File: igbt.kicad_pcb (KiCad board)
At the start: 2 copper layers, 94 parts, among them J1 PWM, J10 Motor, J2 PwrGate_A, J3 PwrGate_B, J4 PwrGate_C, J5 PWM, J6 PWM, J7 Sense_AC_B, J8 Sense_AC_A, J9 DC_Sense, Q1 IRG4PF50W, Q2 IRG4PF50W, Q3 IRG4PF50W, Q4 IRG4PF50W, Q5 IRG4PF50W, Q6 IRG4PF50W, U1 ACS758xCB-050B-PFF, U10 TC4420, U11 6N137, U12 TC4420, U13 6N137, U14 TC4420, U2 ACS758xCB-050B-PFF, U3 6N137, U4 TC4420, U5 6N137, U6 TC4420, U7 6N137, U8 TC4420, U9 6N137

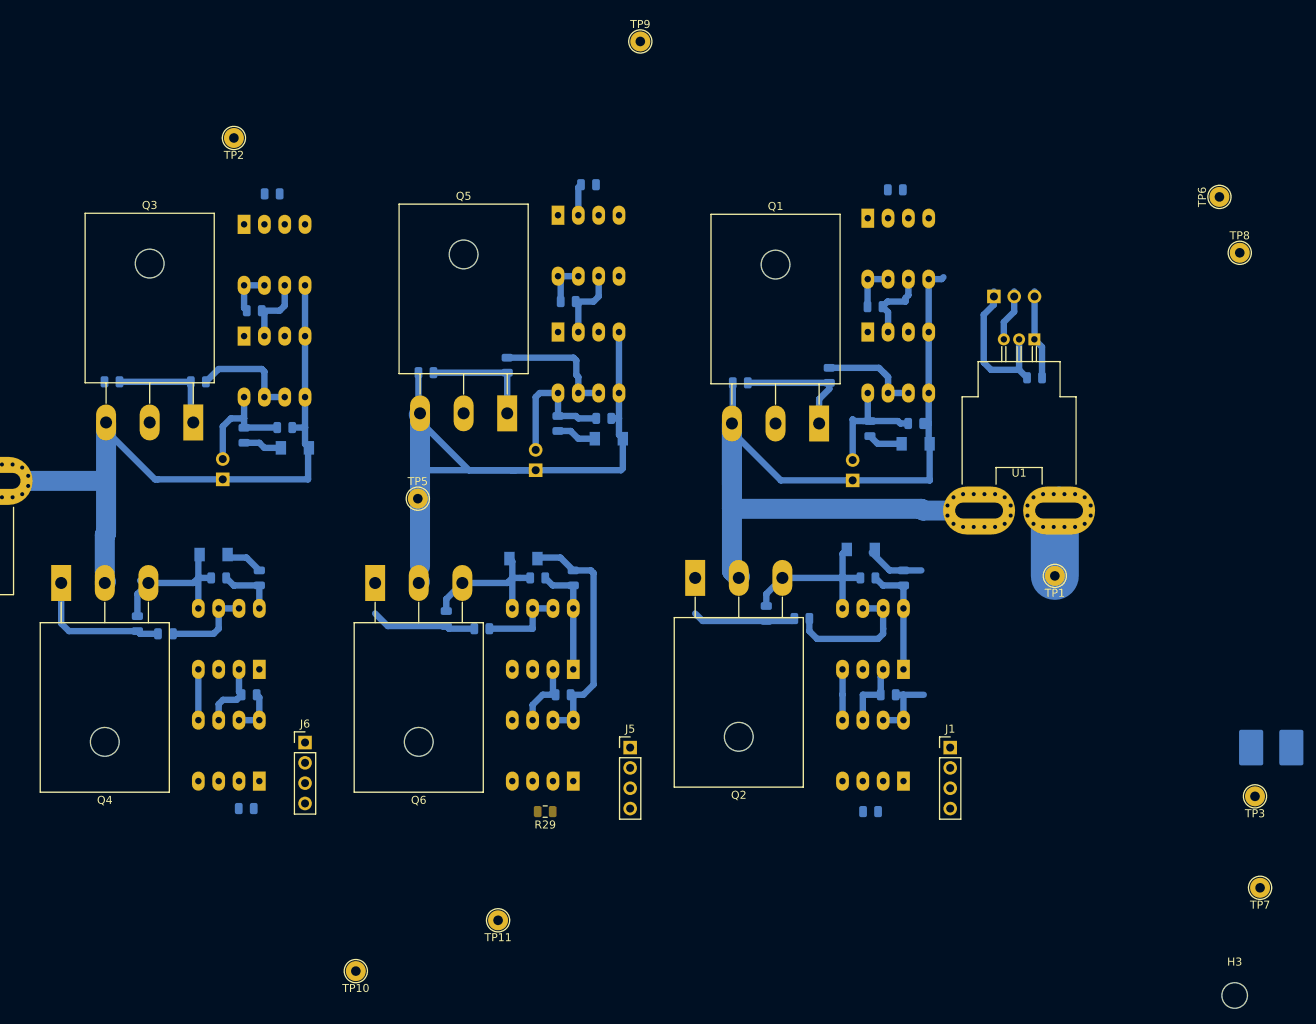
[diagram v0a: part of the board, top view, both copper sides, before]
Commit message: Bus capacitors
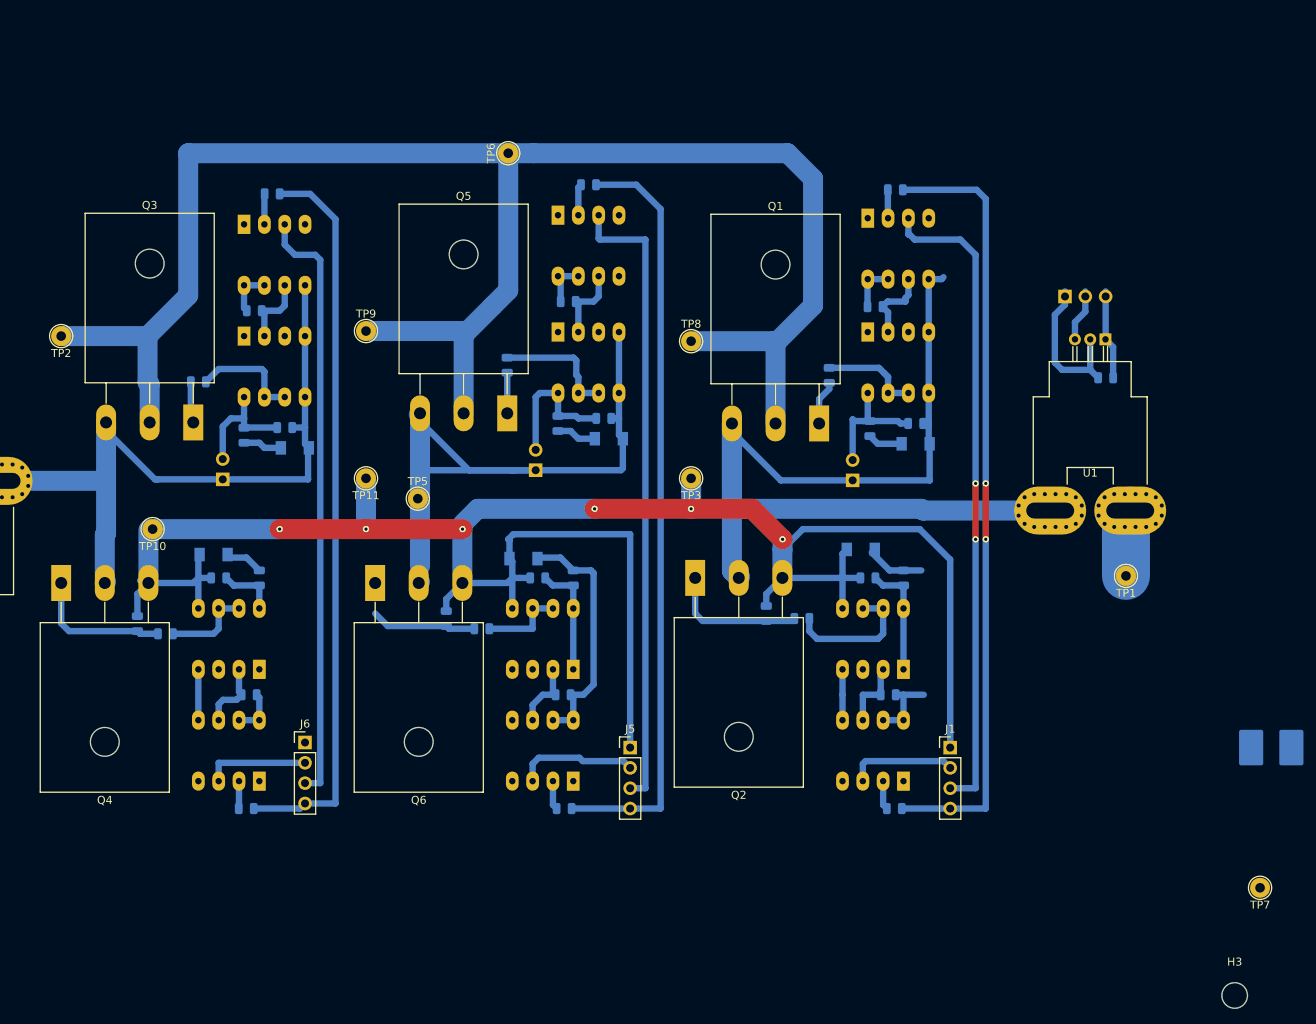
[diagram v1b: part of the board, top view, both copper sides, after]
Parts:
- removed R1, R3, R5: R, Capacitor_SMD:C_0805_2012Metric
- R29: moved to B.Cu
- moved TP6 89.1 mm to (148.0, 50.2)
- moved TP3 80.9 mm to (170.8, 90.8)
- moved TP8 69.5 mm to (170.8, 73.7)
- moved TP10 60.8 mm to (103.5, 97.2)
- moved TP11 57.7 mm to (130.2, 90.8)
- moved TP9 49.9 mm to (130.2, 72.4)
- moved TP2 32.9 mm to (92.1, 73.0)
- moved U1 8.89 mm to (222.6, 73.4)
- moved C4 8.89 mm to (222.6, 78.2)
- moved J8 8.89 mm to (217.6, 68.1)
- moved TP1 8.89 mm to (225.2, 103.0)
- moved R23 2.99 mm to (196.2, 132.1), turned to 0 degrees
- moved R29 2.39 mm to (154.9, 132.1), turned to 0 degrees
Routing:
- net Net-(Q1-Pad2): track 0.71 -> 215.2 mm
- net /DC_Link_GND: track 74.4 -> 276.8 mm, vias 0 -> 6
- net /TopDriver/PowerLed: track 0.00 -> 97.5 mm, vias 0 -> 2
- net /sheet5F5616DC/PowerLed: track 0.00 -> 95.4 mm
- net /sheet5F55AA82/PowerLed: track 0.00 -> 91.8 mm
- net /TopDriver/Cathode: track 0.00 -> 81.3 mm, vias 0 -> 2
- net /sheet5F5616DC/Cathode: track 0.00 -> 79.3 mm
- net /sheet5F55AA82/Cathode: track 0.00 -> 75.1 mm
- net /sheet5F64C50D/Cathode: track 0.00 -> 15.2 mm
- net /sheet5F641D5F/Cathode: track 0.00 -> 13.6 mm
- net /sheet5F647249/Cathode: track 0.00 -> 13.1 mm
- net Net-(Q1-Pad1): track 15.8 -> 5.61 mm
- net Net-(Q5-Pad1): track 14.3 -> 5.08 mm
- net Net-(Q3-Pad1): track 14.1 -> 5.21 mm
- net /sheet5F5616DC/Source: track 86.9 -> 82.0 mm
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
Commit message: Reroute driver tracks
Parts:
- removed J9: DC_Sense, Connector_PinHeader_2.54mm:PinHeader_1x02_P2.54mm_Vertical
- removed R32: 1k, Resistor_SMD:R_2816_7142Metric
- removed R8: 100k, Resistor_SMD:R_2816_7142Metric
- removed TP7: DC_GND, TestPoint:TestPoint_THTPad_D2.5mm_Drill1.2mm
- removed U1: ACS758xCB-050B-PFF, Sensor_Current:Allegro_CB_PFF
- J1, J5, J6: moved to B.Cu
- moved H1 103.5 mm to (48.9, 153.7)
- moved H2 103.5 mm to (36.2, 153.0)
- moved TP14 86.4 mm to (84.5, 72.4)
- moved J10 85.7 mm to (85.1, 60.3)
- moved TP12 85.7 mm to (85.1, 55.2)
- moved TP13 85.7 mm to (80.0, 63.5)
- moved TP4 10.2 mm to (78.4, 74.4)
- moved U2 10.2 mm to (82.2, 103.6)
- moved C5 6.38 mm to (83.2, 106.0)
- moved C4 5.75 mm to (216.9, 78.9)
- moved TP1 5.75 mm to (219.5, 103.6)
- moved J8 5.75 mm to (211.8, 68.7)
- moved J5 3.17 mm to (160.0, 124.5), turned to 180 degrees
- moved J6 2.01 mm to (120.7, 124.5), turned to 180 degrees
- moved J1 1.91 mm to (201.3, 124.5), turned to 180 degrees
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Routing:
- net /DC_Link_GND: track 276.8 -> 342.3 mm
- net Net-(J7-Pad2): track 6.99 -> 40.4 mm
- net /TopDriver/Cathode: track 81.3 -> 108.1 mm, vias 2 -> 0
- net /TopDriver/PowerLed: track 97.5 -> 116.1 mm, vias 2 -> 0
- net Net-(C5-Pad2): track 9.44 -> 19.4 mm
- net /TopDriver/Source: track 135.0 -> 126.1 mm
- net /sheet5F5616DC/Source: track 82.0 -> 88.7 mm
- net /sheet5F55AA82/Source: track 87.7 -> 81.3 mm
- net Net-(D4-Pad1): track 16.4 -> 11.6 mm
- net Net-(Q1-Pad2): track 215.2 -> 211.4 mm
- net Net-(Q6-Pad1): track 13.2 -> 17.0 mm
- net /sheet5F64C50D/Cathode: track 15.2 -> 12.0 mm
- net Net-(J10-Pad3): track 7.50 -> 5.33 mm
- net /sheet5F55AA82/Cathode: track 75.1 -> 76.9 mm
- net /sheet5F641D5F/Cathode: track 13.6 -> 12.0 mm
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
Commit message: Board edge
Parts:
- added TP7: DC_GND, TestPoint:TestPoint_THTPad_D2.5mm_Drill1.2mm, F.Cu at (144.8, 94.0)
- added U1: ACS758xCB-050B-PFF, Sensor_Current:Allegro_CB_PFF, F.Cu at (211.5, 73.7)
- J8: moved to F.Cu
- moved H4 214.0 mm to (76.2, 49.5)
- moved H2 190.7 mm to (225.4, 129.5)
- moved H3 106.8 mm to (225.4, 49.5)
- moved H1 36.4 mm to (76.2, 129.5)
- moved D2 25.2 mm to (110.0, 64.5), turned to 180 degrees
- moved D1 24.8 mm to (186.9, 64.8), turned to 180 degrees
- moved D3 23.9 mm to (149.4, 64.8), turned to 180 degrees
- moved D5 22.1 mm to (103.6, 121.2), turned to 0 degrees
- moved D4 20.7 mm to (185.5, 119.3), turned to 270 degrees
- moved C1 19.5 mm to (186.1, 69.2), turned to 0 degrees
- moved R28 18.8 mm to (102.0, 114.8), turned to 270 degrees
- moved D6 18.1 mm to (145.0, 118.2), turned to 270 degrees
- moved R19 17.4 mm to (111.8, 68.3), turned to 90 degrees
- moved R12 17.0 mm to (189.2, 68.1), turned to 90 degrees
- moved C2 16.4 mm to (109.2, 72.1), turned to 0 degrees
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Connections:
- U10 pad 3: Net-(U10-Pad3) -> (no net)
- U11 pad 1: Net-(U11-Pad1) -> (no net)
- U11 pad 4: Net-(U11-Pad4) -> (no net)
- U12 pad 3: Net-(U12-Pad3) -> (no net)
- U13 pad 1: Net-(U13-Pad1) -> (no net)
- U13 pad 4: Net-(U13-Pad4) -> (no net)
- U14 pad 3: Net-(U14-Pad3) -> (no net)
- U3 pad 1: Net-(U3-Pad1) -> (no net)
- U3 pad 4: Net-(U3-Pad4) -> (no net)
- U4 pad 3: Net-(U4-Pad3) -> (no net)
- U5 pad 1: Net-(U5-Pad1) -> (no net)
- U5 pad 4: Net-(U5-Pad4) -> (no net)
- U6 pad 3: Net-(U6-Pad3) -> (no net)
- U7 pad 1: Net-(U7-Pad1) -> (no net)
- U7 pad 4: Net-(U7-Pad4) -> (no net)
- U8 pad 3: Net-(U8-Pad3) -> (no net)
- U9 pad 1: Net-(U9-Pad1) -> (no net)
- U9 pad 4: Net-(U9-Pad4) -> (no net)
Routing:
- net /sheet5F5616DC/Source: track 88.7 -> 118.5 mm
- net /sheet5F55AA82/Source: track 81.3 -> 103.2 mm
- net Net-(D5-Pad1): track 10.5 -> 31.2 mm, vias 0 -> 2
- net /sheet5F647249/Power: track 7.43 -> 27.0 mm
- net /sheet5F55AA82/Power: track 15.1 -> 31.7 mm, vias 0 -> 2
- net /TopDriver/Power: track 15.8 -> 32.2 mm, vias 0 -> 2
- net /TopDriver/Source: track 126.1 -> 141.9 mm
- net Net-(D4-Pad1): track 11.6 -> 26.0 mm, vias 0 -> 2
- net /sheet5F5616DC/Power: track 17.4 -> 26.7 mm, vias 0 -> 2
- net /sheet5F641D5F/Power: track 14.4 -> 23.3 mm
- net /sheet5F64C50D/Power: track 14.4 -> 22.3 mm
- net Net-(J8-Pad2): track 6.53 -> 13.9 mm
- net /DC_Link_GND: track 342.3 -> 348.2 mm
- net Net-(D6-Pad1): track 31.1 -> 25.7 mm, vias 0 -> 2
- net /TopDriver/PowerLed: track 116.1 -> 120.7 mm
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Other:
- board outline added: 159.4 x 90.2 mm

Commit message: Fill flooded
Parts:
- J8: moved to B.Cu
- moved TP13 8.91 mm to (88.9, 64.1)
- moved R25 4.51 mm to (181.0, 114.5)
- moved R31 4.39 mm to (141.0, 114.9)
- moved D6 3.74 mm to (142.9, 121.3), turned to 0 degrees
- moved D4 3.26 mm to (182.9, 121.3), turned to 0 degrees
- moved R17 1.62 mm to (149.2, 77.5), turned to 0 degrees
- moved J4 1.02 mm to (151.4, 90.8)
- turned J8 to 180 degrees
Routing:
- net Net-(D4-Pad1): track 26.0 -> 34.2 mm
- net Net-(J7-Pad2): track 40.4 -> 48.3 mm
- net /sheet5F5616DC/Source: track 118.5 -> 110.6 mm
- net Net-(C5-Pad1): track 15.3 -> 22.4 mm
- net Net-(D6-Pad1): track 25.7 -> 32.6 mm
- net Net-(C4-Pad2): track 24.0 -> 29.3 mm
- net /TopDriver/Source: track 141.9 -> 147.1 mm
- net /sheet5F64C50D/Power: track 22.3 -> 27.1 mm
- net /sheet5F641D5F/Power: track 23.3 -> 27.8 mm
- net /DC_Link_GND: track 348.2 -> 352.0 mm
- net /TopDriver/PowerLed: track 120.7 -> 123.9 mm
- net /TopDriver/Cathode: track 108.1 -> 110.5 mm
- net /sheet5F5616DC/Gate: track 13.5 -> 11.8 mm
- net /sheet5F55AA82/PowerLed: track 90.3 -> 92.0 mm
- net /sheet5F55AA82/Gate: track 13.8 -> 12.3 mm
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- added copper zone on B.Cu, net (none)
- added copper zone on B.Cu, net /DC_Link_GND
- added copper zone on B.Cu, net Net-(Q1-Pad2)

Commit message: Use adum1300
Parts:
- removed D4, D5, D6: 5V1, Diode_SMD:D_MiniMELF
- removed J3: PwrGate_B, Connector_PinHeader_2.54mm:PinHeader_1x02_P2.54mm_Vertical
- removed J4: PwrGate_C, Connector_PinHeader_2.54mm:PinHeader_1x02_P2.54mm_Vertical
- removed J5, J6: PWM, Connector_PinHeader_2.54mm:PinHeader_1x04_P2.54mm_Vertical
- removed R12, R18, R19, R21, R22, R24, R25, R27, R28, R30, R31, R9: 1k, Resistor_SMD:R_0805_2012Metric
- removed R13, R14, R4, R6: R, Capacitor_SMD:C_0805_2012Metric
- removed R15, R20, R23, R26, R29, R7: 330, Resistor_SMD:R_0805_2012Metric
- removed TP10: DC_CapB_N, TestPoint:TestPoint_THTPad_D2.5mm_Drill1.2mm
- removed TP11: DC_CapC_N, TestPoint:TestPoint_THTPad_D2.5mm_Drill1.2mm
- removed TP2: DC_CapB_P, TestPoint:TestPoint_THTPad_D2.5mm_Drill1.2mm
- removed TP3: DC_CapA_N, TestPoint:TestPoint_THTPad_D2.5mm_Drill1.2mm
- removed TP5: C, TestPoint:TestPoint_THTPad_D2.5mm_Drill1.2mm
- removed TP6: DC_BUS, TestPoint:TestPoint_THTPad_D2.5mm_Drill1.2mm
- removed TP7: DC_GND, TestPoint:TestPoint_THTPad_D2.5mm_Drill1.2mm
- removed TP8: DC_CapA_P, TestPoint:TestPoint_THTPad_D2.5mm_Drill1.2mm
- removed TP9: DC_CapC_P, TestPoint:TestPoint_THTPad_D2.5mm_Drill1.2mm
- removed U10, U12, U14, U8: TC4420, Package_DIP:DIP-8_W7.62mm_LongPads
- removed U11, U13, U9: 6N137, Package_DIP:DIP-8_W7.62mm_LongPads
- added J9: DC_Sense, Connector_PinHeader_2.54mm:PinHeader_1x02_P2.54mm_Vertical, F.Cu at (55.2, 42.5)
- added R1: R, Capacitor_SMD:C_0805_2012Metric, B.Cu at (94.0, 108.0)
- added R32: 1k, Resistor_SMD:R_2816_7142Metric, B.Cu at (49.4, 45.0)
- added R8: 100k, Resistor_SMD:R_2816_7142Metric, B.Cu at (49.4, 40.0)
- D1, D2, D3: value 5V1 -> DIODE; footprint Diode_SMD:D_MiniMELF -> Diode_THT:D_A-405_P2.54mm_Vertical_KathodeUp
- J1: footprint Connector_PinHeader_2.54mm:PinHeader_1x04_P2.54mm_Vertical -> Connector_PinHeader_2.54mm:PinHeader_1x08_P2.54mm_Vertical
- J2: value PwrGate_A -> V_Gate
- U3: value 6N137 -> ADum1300; footprint Package_DIP:DIP-8_W7.62mm_LongPads -> Package_SO:SOIC-16W_7.5x10.3mm_P1.27mm
- U4: value TC4420 -> ADum1300; footprint Package_DIP:DIP-8_W7.62mm_LongPads -> Package_SO:SOIC-16W_7.5x10.3mm_P1.27mm
- U5, U7: value 6N137 -> IR2110; footprint Package_DIP:DIP-8_W7.62mm_LongPads -> Package_SO:SOIC-16W_7.5x10.3mm_P1.27mm
- U6: value TC4420 -> IR2110; footprint Package_DIP:DIP-8_W7.62mm_LongPads -> Package_SO:SOIC-16W_7.5x10.3mm_P1.27mm
- moved H2 168.8 mm to (124.5, -5.71)
- moved H1 154.7 mm to (138.4, -12.1)
- moved H3 129.3 mm to (108.0, -4.45)
- moved C6 106.1 mm to (91.4, 102.9)
- moved R2 87.6 mm to (94.0, 92.1), turned to 270 degrees
- moved U3 73.3 mm to (150.9, 118.4), turned to 90 degrees
- moved C3 63.3 mm to (91.4, 99.1), turned to 270 degrees
- moved H4 61.3 mm to (96.5, -8.26)
- moved C1 58.7 mm to (134.9, 97.9), turned to 270 degrees
- moved J10 56.0 mm to (29.2, 64.1)
- moved TP12 56.0 mm to (29.2, 59.1)
- moved TP13 56.0 mm to (33.0, 67.9)
- moved C4 55.3 mm to (267.1, 82.0)
- moved J8 55.3 mm to (273.1, 74.9)
- moved TP1 55.3 mm to (269.2, 104.1)
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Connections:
- C1 pad 1: /TopDriver/Source -> Net-(C1-Pad1)
- C1 pad 2: /TopDriver/Power -> Net-(C1-Pad2)
- C2 pad 1: /sheet5F55AA82/Source -> Net-(C2-Pad1)
- C2 pad 2: /sheet5F55AA82/Power -> /DC_Link_GND
- C3 pad 1: /sheet5F5616DC/Source -> Net-(C3-Pad1)
- C3 pad 2: /sheet5F5616DC/Power -> Net-(C3-Pad2)
- C6 pad 1: /DC_Link_GND -> Net-(C2-Pad1)
- C6 pad 2: /sheet5F641D5F/Power -> /DC_Link_GND
- C7 pad 1: /DC_Link_GND -> Net-(C7-Pad1)
- C7 pad 2: /sheet5F647249/Power -> Net-(C7-Pad2)
- C8 pad 1: /DC_Link_GND -> Net-(C2-Pad1)
- C8 pad 2: /sheet5F64C50D/Power -> /DC_Link_GND
- D1 pad 1: Net-(D1-Pad1) -> Net-(C2-Pad1)
- D1 pad 2: /TopDriver/Source -> Net-(C1-Pad1)
- D2 pad 1: Net-(D2-Pad1) -> Net-(C2-Pad1)
- D2 pad 2: /sheet5F55AA82/Source -> Net-(C3-Pad1)
- D3 pad 1: Net-(D3-Pad1) -> Net-(C2-Pad1)
- D3 pad 2: /sheet5F5616DC/Source -> Net-(C7-Pad1)
- J1 pad 1: /DC_Link_GND -> Net-(J1-Pad1)
- J1 pad 2: /sheet5F641D5F/Cathode -> Net-(J1-Pad2)
- J1 pad 3: /TopDriver/Cathode -> Net-(J1-Pad3)
- J1 pad 4: /TopDriver/PowerLed -> Net-(J1-Pad4)
- J2 pad 1: /TopDriver/Source -> Net-(J2-Pad1)
- J2 pad 2: /TopDriver/Power -> Net-(C2-Pad1)
- Q1 pad 3: /TopDriver/Source -> Net-(C1-Pad2)
- Q2 pad 2: /TopDriver/Source -> Net-(C1-Pad2)
- Q3 pad 3: /sheet5F55AA82/Source -> Net-(C3-Pad2)
- Q4 pad 2: /sheet5F55AA82/Source -> Net-(C3-Pad2)
- Q5 pad 3: /sheet5F5616DC/Source -> Net-(C7-Pad2)
- Q6 pad 2: /sheet5F5616DC/Source -> Net-(C7-Pad2)
- R10 pad 2: /sheet5F641D5F/Gate -> Net-(R10-Pad2)
- R11 pad 2: /TopDriver/Gate -> Net-(R11-Pad2)
- R16 pad 2: /sheet5F64C50D/Gate -> Net-(R16-Pad2)
- R17 pad 2: /sheet5F5616DC/Gate -> Net-(R17-Pad2)
- R2 pad 1: Net-(Q2-Pad1) -> Net-(Q3-Pad1)
- R2 pad 2: /DC_Link_GND -> Net-(R2-Pad2)
- U1 pad 4: /TopDriver/Source -> Net-(C1-Pad2)
- U2 pad 4: /sheet5F55AA82/Source -> Net-(C3-Pad2)
- U3 pad 1: (no net) -> Net-(J1-Pad8)
- U3 pad 2: Net-(R7-Pad1) -> Net-(J1-Pad8)
- U3 pad 3: /TopDriver/Cathode -> Net-(J1-Pad4)
- U3 pad 4: (no net) -> Net-(J1-Pad3)
- U3 pad 5: /TopDriver/Source -> Net-(J1-Pad2)
- U3 pad 6: Net-(R9-Pad2) -> Net-(U3-Pad6)
- U3 pad 7: Net-(D1-Pad1) -> Net-(U3-Pad7)
- U3 pad 8: Net-(D1-Pad1) -> Net-(J1-Pad1)
- U4 pad 1: /TopDriver/Power -> Net-(J1-Pad8)
- U4 pad 2: Net-(R9-Pad2) -> Net-(J1-Pad1)
- U4 pad 3: (no net) -> Net-(J1-Pad7)
- U4 pad 4: /TopDriver/Source -> Net-(J1-Pad6)
- U4 pad 5: /TopDriver/Source -> Net-(J1-Pad5)
- U4 pad 6: /TopDriver/Gate -> Net-(U4-Pad6)
- U4 pad 7: /TopDriver/Gate -> Net-(U4-Pad7)
- U4 pad 8: /TopDriver/Power -> Net-(J1-Pad1)
- U5 pad 1: (no net) -> Net-(R10-Pad2)
- U5 pad 2: Net-(R15-Pad1) -> /DC_Link_GND
- U5 pad 3: /sheet5F55AA82/Cathode -> Net-(C2-Pad1)
- U5 pad 4: (no net) -> Net-(U5-Pad4)
- U5 pad 5: /sheet5F55AA82/Source -> Net-(C1-Pad2)
- U5 pad 6: Net-(R18-Pad2) -> Net-(C1-Pad1)
- U5 pad 7: Net-(D2-Pad1) -> Net-(R11-Pad2)
- U5 pad 8: Net-(D2-Pad1) -> Net-(U5-Pad8)
- U6 pad 1: /sheet5F55AA82/Power -> Net-(R1-Pad2)
- U6 pad 2: Net-(R18-Pad2) -> /DC_Link_GND
- U6 pad 3: (no net) -> Net-(C2-Pad1)
- U6 pad 4: /sheet5F55AA82/Source -> Net-(U6-Pad4)
- U6 pad 5: /sheet5F55AA82/Source -> Net-(C3-Pad2)
- U6 pad 6: /sheet5F55AA82/Gate -> Net-(C3-Pad1)
- U6 pad 7: /sheet5F55AA82/Gate -> Net-(R2-Pad2)
- U6 pad 8: /sheet5F55AA82/Power -> Net-(U6-Pad8)
- U7 pad 1: (no net) -> Net-(R16-Pad2)
- U7 pad 2: Net-(R20-Pad1) -> /DC_Link_GND
- U7 pad 3: /sheet5F5616DC/Cathode -> Net-(C2-Pad1)
- U7 pad 4: (no net) -> Net-(U7-Pad4)
- U7 pad 5: /sheet5F5616DC/Source -> Net-(C7-Pad2)
- U7 pad 6: Net-(R21-Pad2) -> Net-(C7-Pad1)
- U7 pad 7: Net-(D3-Pad1) -> Net-(R17-Pad2)
- U7 pad 8: Net-(D3-Pad1) -> Net-(U7-Pad8)
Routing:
- net /DC_Link_GND: track 352.0 -> 168.0 mm, vias 6 -> 0
- net Net-(Q1-Pad2): track 211.4 -> 63.2 mm
- net /TopDriver/Source: track 147.1 -> 0.00 mm
- net /TopDriver/PowerLed: track 123.9 -> 0.00 mm
- net Net-(C2-Pad1): track 0.00 -> 113.9 mm, vias 0 -> 4
- net /sheet5F5616DC/Source: track 110.6 -> 0.00 mm
- net /TopDriver/Cathode: track 110.5 -> 0.00 mm
- net Net-(J2-Pad1): track 0.00 -> 107.7 mm, vias 0 -> 4
- net /sheet5F55AA82/Source: track 103.2 -> 0.00 mm
- net /sheet5F5616DC/PowerLed: track 94.7 -> 0.00 mm
- net /sheet5F55AA82/PowerLed: track 92.0 -> 0.00 mm
- net /sheet5F5616DC/Cathode: track 81.4 -> 0.00 mm
- net /sheet5F55AA82/Cathode: track 76.9 -> 0.00 mm
- net Net-(C7-Pad2): track 0.00 -> 75.2 mm
- net Net-(C3-Pad2): track 0.00 -> 74.0 mm
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- removed copper zone on B.Cu, net (none)
- removed copper zone on B.Cu, net /DC_Link_GND
- removed copper zone on B.Cu, net Net-(Q1-Pad2)
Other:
- board outline removed

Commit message: only gate drivers, no opto
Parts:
- removed U3, U4: ADum1300, Package_SO:SOIC-16W_7.5x10.3mm_P1.27mm
- D1: footprint Diode_THT:D_A-405_P2.54mm_Vertical_KathodeUp -> Diode_THT:D_A-405_P7.62mm_Horizontal
- moved C4 104.1 mm to (164.5, 64.8)
- moved J8 104.1 mm to (170.4, 57.7)
- moved TP1 104.1 mm to (166.6, 86.9)
- moved U1 104.1 mm to (164.1, 59.6)
- moved U2 40.1 mm to (71.9, 111.8)
- moved J7 40.1 mm to (73.5, 126.9)
- moved TP4 40.1 mm to (68.1, 82.5)
- moved C5 40.1 mm to (72.9, 114.2)
- moved J2 30.6 mm to (141.7, 121.9)
- moved D1 19.2 mm to (126.5, 90.4), turned to 0 degrees
- moved R11 14.7 mm to (143.8, 76.7), turned to 0 degrees
- moved R10 13.0 mm to (126.2, 110.6)
- moved J1 12.4 mm to (146.6, 117.3)
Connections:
- J1 pad 2: Net-(J1-Pad2) -> /A_L
- J1 pad 3: Net-(J1-Pad3) -> /A_H
- J1 pad 4: Net-(J1-Pad4) -> /B_L
- J1 pad 5: Net-(J1-Pad5) -> /B_H
- J1 pad 6: Net-(J1-Pad6) -> /C_L
- J1 pad 7: Net-(J1-Pad7) -> /C_H
- J2 pad 1: Net-(J2-Pad1) -> Net-(J1-Pad1)
- U5 pad 11: Net-(U5-Pad11) -> (no net)
- U5 pad 13: Net-(J2-Pad1) -> Net-(J1-Pad1)
- U5 pad 14: Net-(U5-Pad14) -> (no net)
- U5 pad 4: Net-(U5-Pad4) -> (no net)
- U5 pad 8: Net-(U5-Pad8) -> (no net)
- U5 pad 9: Net-(U3-Pad16) -> Net-(J1-Pad8)
- U6 pad 11: Net-(U6-Pad11) -> (no net)
- U6 pad 13: Net-(J2-Pad1) -> Net-(J1-Pad1)
- U6 pad 14: Net-(U6-Pad14) -> (no net)
- U6 pad 4: Net-(U6-Pad4) -> (no net)
- U6 pad 8: Net-(U6-Pad8) -> (no net)
- U6 pad 9: Net-(U6-Pad9) -> Net-(J1-Pad8)
- U7 pad 11: Net-(U7-Pad11) -> (no net)
- U7 pad 13: Net-(J2-Pad1) -> Net-(J1-Pad1)
- U7 pad 14: Net-(U7-Pad14) -> (no net)
- U7 pad 4: Net-(U7-Pad4) -> (no net)
- U7 pad 8: Net-(U7-Pad8) -> (no net)
- U7 pad 9: Net-(U7-Pad9) -> Net-(J1-Pad8)
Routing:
- net Net-(J2-Pad1): track 107.7 -> 0.00 mm, vias 4 -> 0
- net Net-(J1-Pad1): track 12.6 -> 88.5 mm, vias 0 -> 3
- net Net-(J1-Pad8): track 30.6 -> 89.5 mm, vias 0 -> 6
- net Net-(U3-Pad16): track 47.1 -> 0.00 mm, vias 4 -> 0
- net Net-(R11-Pad2): track 7.68 -> 30.1 mm, vias 0 -> 2
- net Net-(Q2-Pad1): track 19.6 -> 3.56 mm, vias 2 -> 0
- net Net-(C3-Pad2): track 74.0 -> 89.0 mm
- net Net-(R10-Pad2): track 2.32 -> 16.7 mm, vias 0 -> 2
- net Net-(C2-Pad1): track 113.9 -> 124.7 mm
- net /B_L: track 56.8 -> 67.6 mm
- net Net-(J1-Pad7): track 10.4 -> 0.00 mm
- net Net-(C1-Pad2): track 72.7 -> 82.0 mm
- net /A_H: track 34.9 -> 26.0 mm, vias 2 -> 1
- net /C_L: track 41.1 -> 47.8 mm
- net Net-(Q1-Pad1): track 10.3 -> 4.91 mm
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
